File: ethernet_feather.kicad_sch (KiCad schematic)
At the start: 76 parts, among them J1 USB_C_Receptacle_USB2.0, J2 TC2030-NL, J3 JST PH 2 pin, J4 JST SH4 pin, U1 MIMXRT1051CVJ5B, U2 LP3982IMM-3.3, U3 MCP73831-2-OT, U4 W25Q32JVZP, U5 WE-TVS-82400102, Y1 24MHz 6pF, Y2 32.768kHz

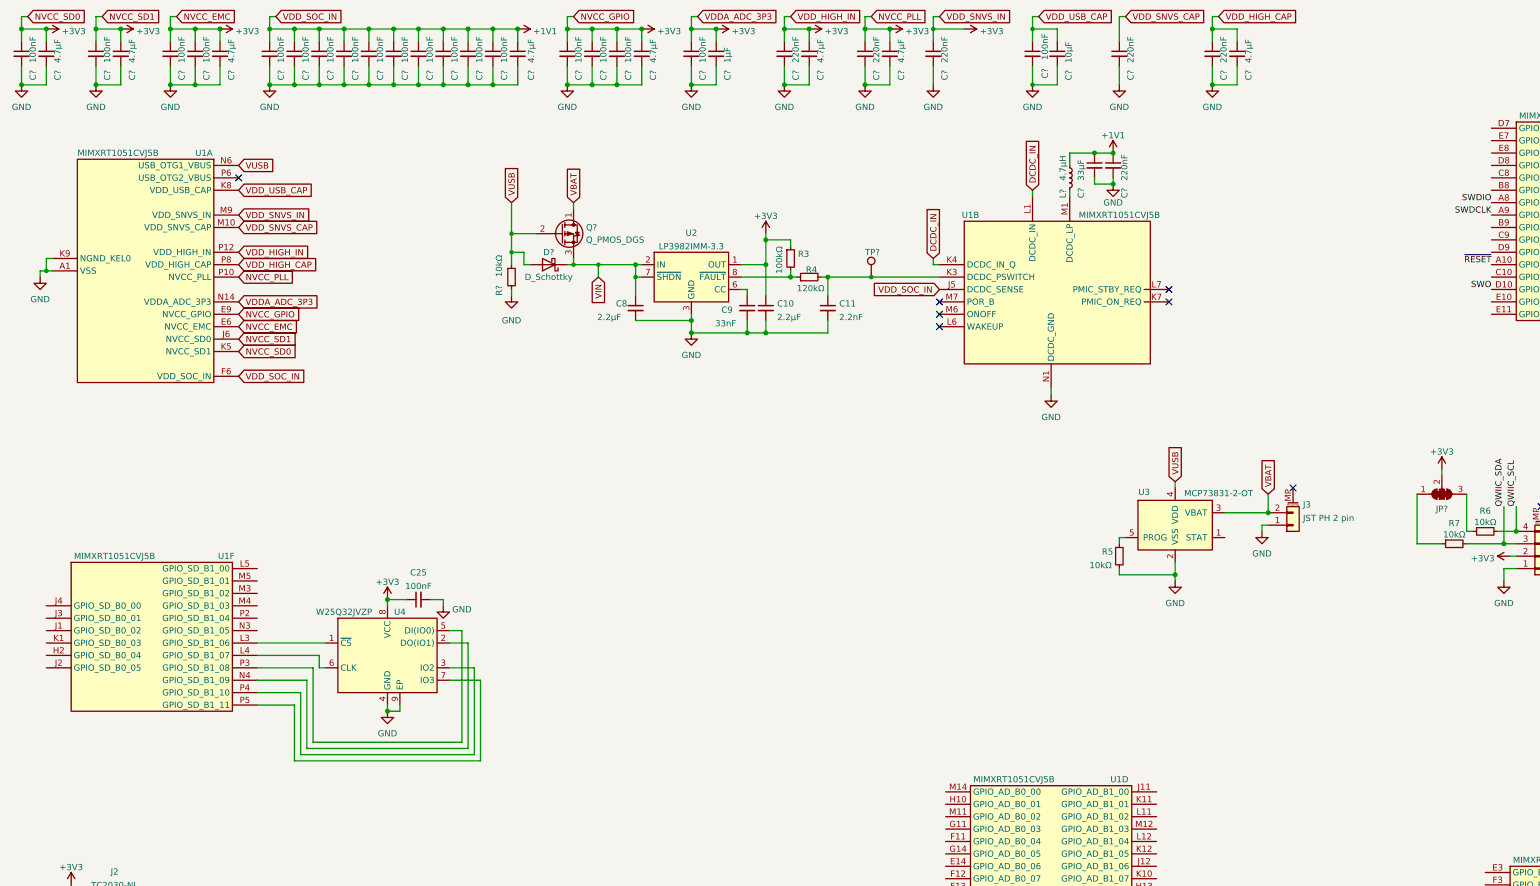
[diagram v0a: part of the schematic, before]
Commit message: Add microSD card and annotate mostly complete schematic
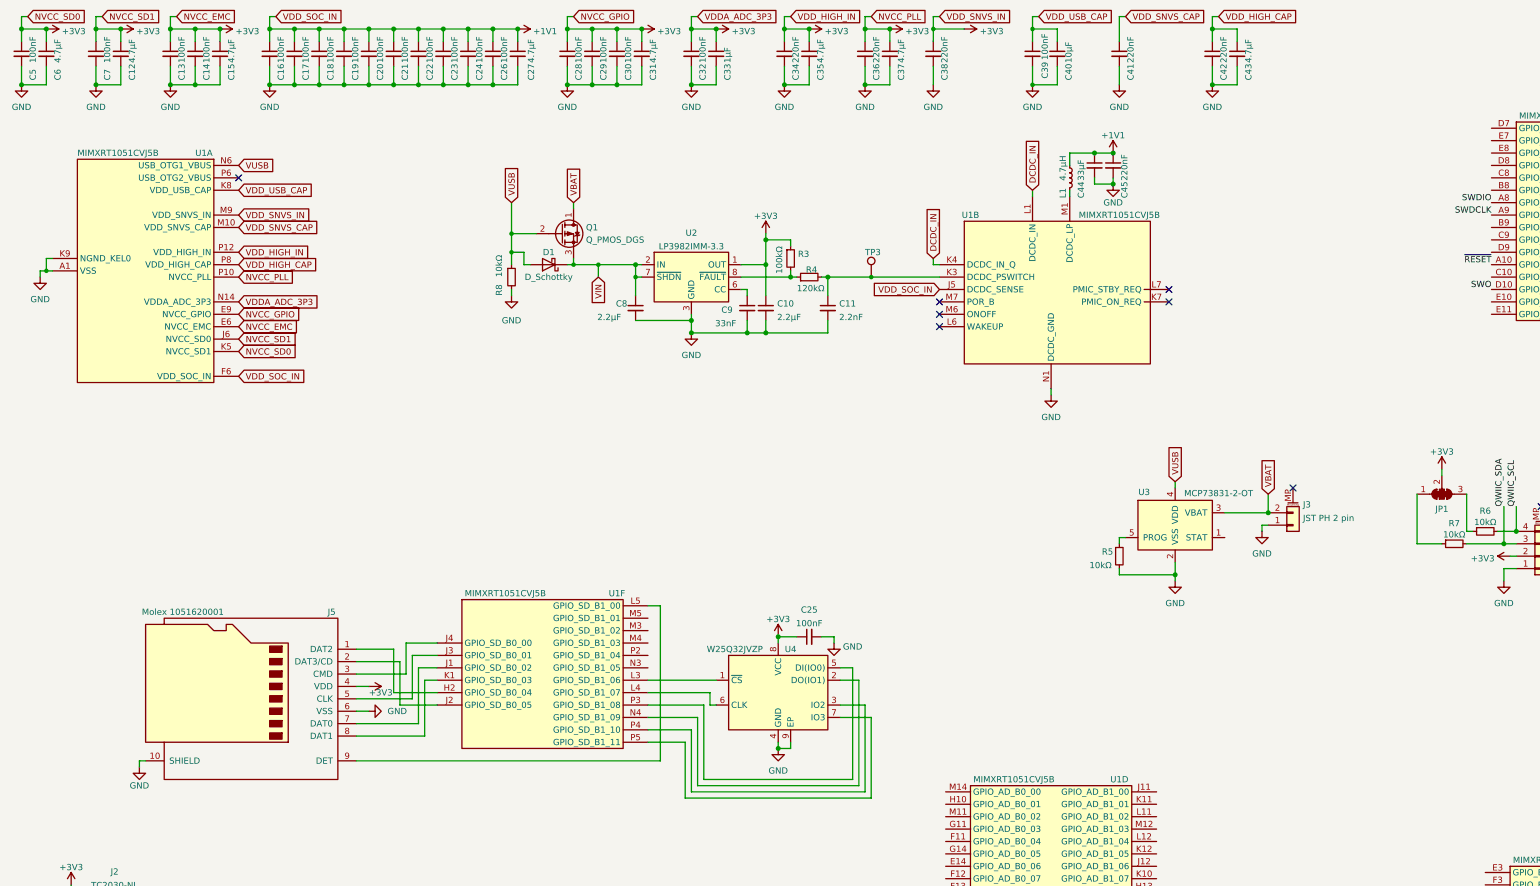
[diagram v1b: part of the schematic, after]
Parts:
- added J5: Molex 1051620001, ethernet_feather:microSD_HC_Molex_1051620001, symbol ethernet_feather:Micro_SD_Card_Det_SH
- C44, C45: renamed from C?; footprint (none) -> Capacitor_SMD:C_0402_1005Metric
- D1: renamed from D?; footprint (none) -> Diode_SMD:D_SOD-323
- L1: renamed from L?; footprint (none) -> Inductor_SMD:L_0603_1608Metric
- Q1: renamed from Q?; footprint (none) -> Package_TO_SOT_SMD:SOT-23
- R8: renamed from R?; footprint (none) -> Resistor_SMD:R_0402_1005Metric
- TP3: renamed from TP?; footprint (none) -> TestPoint:TestPoint_Pad_D1.0mm
- gave numbers to parts that had none: 35
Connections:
- net +3V3: now also J5.4 (VDD)
- net DCDC_GND: now also J5.10 (SHIELD), J5.6 (VSS)
- net at U1.H2 (GPIO_SD_B0_04): now also J5.1 (DAT2)
- net at U1.J1 (GPIO_SD_B0_02): now also J5.7 (DAT0)
- net at U1.J2 (GPIO_SD_B0_05): now also J5.2 (DAT3/CD)
- net at U1.J3 (GPIO_SD_B0_01): now also J5.5 (CLK)
- net at U1.J4 (GPIO_SD_B0_00): now also J5.3 (CMD)
- net at U1.K1 (GPIO_SD_B0_03): now also J5.8 (DAT1)
- net at U1.L5 (GPIO_SD_B1_00): now also J5.9 (DET)
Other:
- moved on the sheet: C25, U1F, U4

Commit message: YOU CAN'T CUT BACK ON DECOUPLING CAPACITORS! YOU WILL REGRET THIS!
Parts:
- C24: footprint Capacitor_SMD:C_0603_1608Metric -> Capacitor_SMD:C_0402_1005Metric

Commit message: Start PCB
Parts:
- removed C18, C19, C20, C21, C22, C23, C26, C30: 100nF, Capacitor_SMD:C_0603_1608Metric, symbol Device:C_Small
- removed C24: 100nF, Capacitor_SMD:C_0402_1005Metric, symbol Device:C_Small
- C1: renamed from C5; footprint Capacitor_SMD:C_0603_1608Metric -> Capacitor_SMD:C_0402_1005Metric
- C10: renamed from C27; footprint Capacitor_SMD:C_0603_1608Metric -> Capacitor_SMD:C_0402_1005Metric
- C11: renamed from C28; footprint Capacitor_SMD:C_0603_1608Metric -> Capacitor_SMD:C_0402_1005Metric
- C12: renamed from C29; footprint Capacitor_SMD:C_0603_1608Metric -> Capacitor_SMD:C_0402_1005Metric
- C13: renamed from C31; footprint Capacitor_SMD:C_0603_1608Metric -> Capacitor_SMD:C_0402_1005Metric
- C14: renamed from C32; footprint Capacitor_SMD:C_0603_1608Metric -> Capacitor_SMD:C_0402_1005Metric
- C15: renamed from C33; footprint Capacitor_SMD:C_0603_1608Metric -> Capacitor_SMD:C_0402_1005Metric
- C16: renamed from C34; footprint Capacitor_SMD:C_0603_1608Metric -> Capacitor_SMD:C_0402_1005Metric
- C17: renamed from C35; footprint Capacitor_SMD:C_0603_1608Metric -> Capacitor_SMD:C_0402_1005Metric
- C18: renamed from C36; footprint Capacitor_SMD:C_0603_1608Metric -> Capacitor_SMD:C_0402_1005Metric
- C19: renamed from C37; footprint Capacitor_SMD:C_0603_1608Metric -> Capacitor_SMD:C_0402_1005Metric
- C2: renamed from C6; footprint Capacitor_SMD:C_0603_1608Metric -> Capacitor_SMD:C_0402_1005Metric
- C20: renamed from C38; footprint Capacitor_SMD:C_0603_1608Metric -> Capacitor_SMD:C_0402_1005Metric
- C21: renamed from C39; footprint Capacitor_SMD:C_0603_1608Metric -> Capacitor_SMD:C_0402_1005Metric
- C22: renamed from C40; footprint Capacitor_SMD:C_0603_1608Metric -> Capacitor_SMD:C_0402_1005Metric
- C23: renamed from C41; footprint Capacitor_SMD:C_0603_1608Metric -> Capacitor_SMD:C_0402_1005Metric
- C24: renamed from C42; footprint Capacitor_SMD:C_0603_1608Metric -> Capacitor_SMD:C_0402_1005Metric
- C25: renamed from C43; footprint Capacitor_SMD:C_0603_1608Metric -> Capacitor_SMD:C_0402_1005Metric
- C28: renamed from C8; footprint Capacitor_SMD:C_0603_1608Metric -> Capacitor_SMD:C_0402_1005Metric
- C29: renamed from C9; footprint Capacitor_SMD:C_0603_1608Metric -> Capacitor_SMD:C_0402_1005Metric
- C3: renamed from C7; footprint Capacitor_SMD:C_0603_1608Metric -> Capacitor_SMD:C_0402_1005Metric
- C30: renamed from C10; footprint Capacitor_SMD:C_0603_1608Metric -> Capacitor_SMD:C_0402_1005Metric
- C31: renamed from C11; footprint Capacitor_SMD:C_0603_1608Metric -> Capacitor_SMD:C_0402_1005Metric
- C32: renamed from C25; footprint Capacitor_SMD:C_0603_1608Metric -> Capacitor_SMD:C_0402_1005Metric
- C33: renamed from C3; footprint Capacitor_SMD:C_0603_1608Metric -> Capacitor_SMD:C_0402_1005Metric
- C34: renamed from C4; footprint Capacitor_SMD:C_0603_1608Metric -> Capacitor_SMD:C_0402_1005Metric
- C35: renamed from C1; footprint Capacitor_SMD:C_0603_1608Metric -> Capacitor_SMD:C_0402_1005Metric
- C36: renamed from C2; footprint Capacitor_SMD:C_0603_1608Metric -> Capacitor_SMD:C_0402_1005Metric
- C4: renamed from C12; footprint Capacitor_SMD:C_0603_1608Metric -> Capacitor_SMD:C_0402_1005Metric
- C5: renamed from C13; footprint Capacitor_SMD:C_0603_1608Metric -> Capacitor_SMD:C_0402_1005Metric
- C6: renamed from C14; footprint Capacitor_SMD:C_0603_1608Metric -> Capacitor_SMD:C_0402_1005Metric
- C7: renamed from C15; footprint Capacitor_SMD:C_0603_1608Metric -> Capacitor_SMD:C_0402_1005Metric
- C8: renamed from C16; footprint Capacitor_SMD:C_0603_1608Metric -> Capacitor_SMD:C_0402_1005Metric
- C9: renamed from C17; footprint Capacitor_SMD:C_0603_1608Metric -> Capacitor_SMD:C_0402_1005Metric
- R1: renamed from R3; footprint Resistor_SMD:R_0603_1608Metric -> Resistor_SMD:R_0402_1005Metric
- R3: renamed from R4; footprint Resistor_SMD:R_0603_1608Metric -> Resistor_SMD:R_0402_1005Metric
- R4: renamed from R6; footprint Resistor_SMD:R_0603_1608Metric -> Resistor_SMD:R_0402_1005Metric
- R5: renamed from R7; footprint Resistor_SMD:R_0603_1608Metric -> Resistor_SMD:R_0402_1005Metric
- R6: renamed from R5; footprint Resistor_SMD:R_0603_1608Metric -> Resistor_SMD:R_0402_1005Metric
- R7: renamed from R1; footprint Resistor_SMD:R_0603_1608Metric -> Resistor_SMD:R_0402_1005Metric
- R8: renamed from R2; footprint Resistor_SMD:R_0603_1608Metric -> Resistor_SMD:R_0402_1005Metric
- renumbered C44 to C26, C45 to C27, H3 to H1, H1 to H2, H2 to H3, J3 to J1, J4 to J2, J5 to J3, J2 to J4, J1 to J5, R8 to R2, TP3 to TP1, TP1 to TP2, TP2 to TP3, Y2 to Y1, Y1 to Y2
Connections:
- net +3V3: now also A1.2 (3V3)
- net VBAT: now also A1.28 (VBAT)
- net VUSB: now also A1.26 (USB)
- net USB_D+: now reaches U1.L8 (USB_OTG1_D+), U5.1
- net USB_D-: now reaches U1.M8 (USB_OTG1_D-), U5.3
- net USB_DIRECT_D+: now reaches J5.A6 (D+), J5.B6 (D+), U5.6
- net USB_DIRECT_D-: now reaches J5.A7 (D-), J5.B7 (D-), U5.4
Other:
- moved on the sheet: C10, C11, C12, C13, C14, C15, C16, C17, C18, C19, C20, C21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

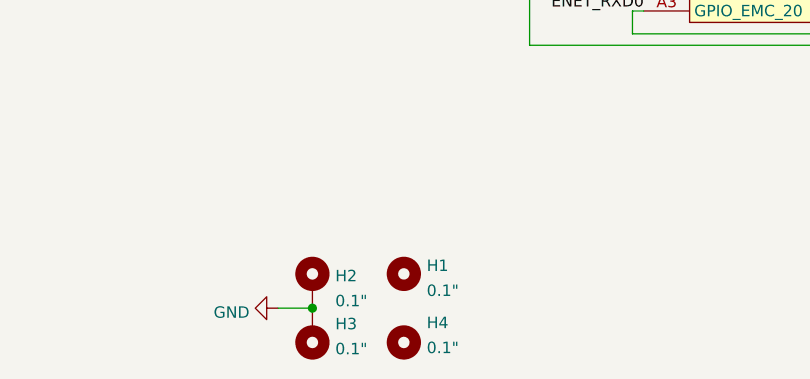
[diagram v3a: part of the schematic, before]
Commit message: Fix up mounting holes, route more flash and microSD
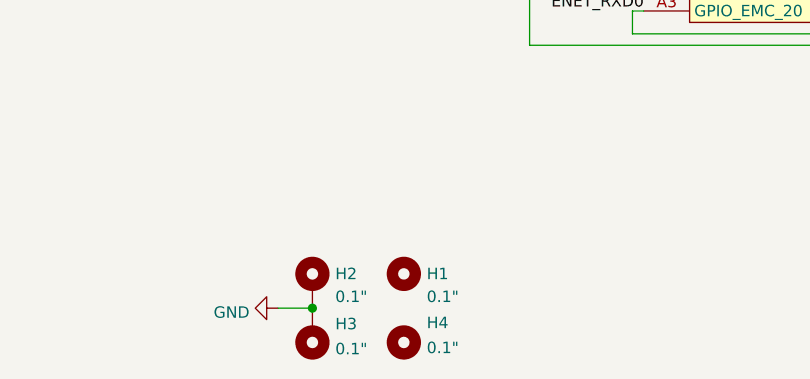
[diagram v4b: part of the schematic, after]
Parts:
- H1, H4: footprint MountingHole:MountingHole_2.5mm -> ethernet_feather:MountingHole_2.5mm_Small
- H2, H3: footprint MountingHole:MountingHole_2.5mm_Pad -> ethernet_feather:MountingHole_2.5mm_Pad_Small

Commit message: Old work, I have no idea what this is
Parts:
- removed C9: 100nF, Capacitor_SMD:C_0402_1005Metric, symbol Device:C_Small
- Y1: footprint Crystal:Crystal_SMD_2520-4Pin_2.5x2.0mm -> Crystal:Crystal_SMD_3215-2Pin_3.2x1.5mm
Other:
- moved on the sheet: C10
